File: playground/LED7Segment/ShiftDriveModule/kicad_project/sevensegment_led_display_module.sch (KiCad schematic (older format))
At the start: 11 parts, among them P1 CONN_01X05, U1 74HC595

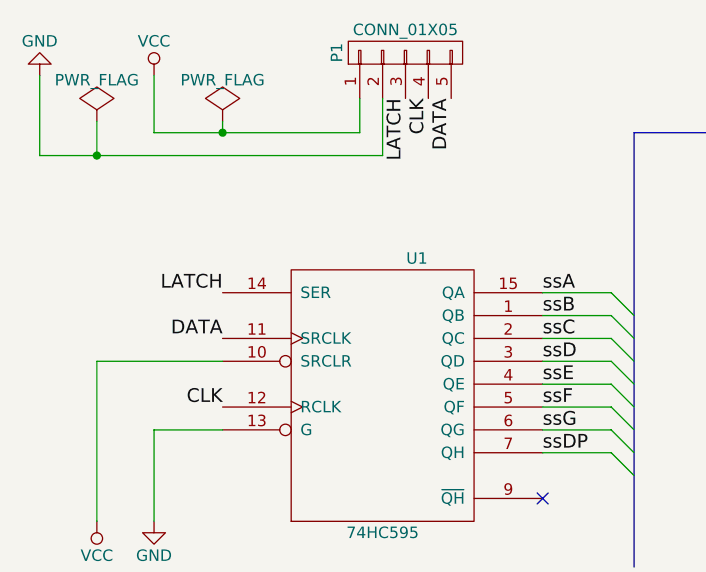
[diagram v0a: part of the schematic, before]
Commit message: [LED7Segment/ShiftDriveModule] update now I have the PCBs from OSHPark
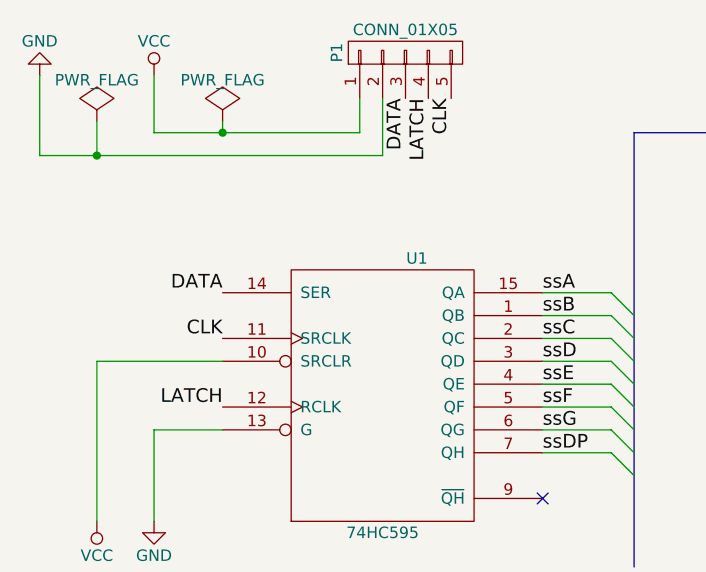
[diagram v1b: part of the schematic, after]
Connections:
- net CLK: now also P1.5 (P5), U1.11 (SRCLK); no longer P1.4 (P4), U1.12 (RCLK)
- net DATA: now also P1.3 (P3), U1.14 (SER); no longer P1.5 (P5), U1.11 (SRCLK)
- net LATCH: now also P1.4 (P4), U1.12 (RCLK); no longer P1.3 (P3), U1.14 (SER)
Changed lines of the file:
@@
 LIBS:contrib
 LIBS:valves
+LIBS:sevensegment_led_display_module-cache
 EELAYER 25 0
 EELAYER END
@@
 Title "Seven-Segment Display Module"
 Date "2016-01-18"
-Rev "1.0.0"
+Rev "1.1.0"
 Comp "github.com/tardate/LittleArduinoProjects"
 Comment1 ""
@@
 	1    0    0    -1
 $EndComp
+Text Label 3500 3050 3    60   ~ 0
+DATA
+Text Label 2700 3900 2    60   ~ 0
+DATA
 Text Label 3700 3050 3    60   ~ 0
-DATA
+CLK
 Text Label 2700 4100 2    60   ~ 0
-DATA
+CLK
 Text Label 3600 3050 3    60   ~ 0
-CLK
+LATCH
 Text Label 2700 4400 2    60   ~ 0
-CLK
-Text Label 3500 3050 3    60   ~ 0
-LATCH
-Text Label 2700 3900 2    60   ~ 0
 LATCH
 $Comp
